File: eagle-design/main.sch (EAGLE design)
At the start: 16 parts, among them IC1 7805T

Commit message: Added new code
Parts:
- added R5, R6: 10K, adafruit:FLIPFLOP-RES
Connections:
- new net VCC: R5.1, R6.1
- net N$7: now also R6.2
- net N$8: now also R5.2
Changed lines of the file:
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@@
 <part name="S1" library="switch-omron" library_urn="urn:adsk.eagle:library:377" deviceset="10-XX" device="" package3d_urn="urn:adsk.eagle:package:27496/1"/>
 <part name="R4" library="adafruit" deviceset="FLIPFLOP-RES" device="" value="10K"/>
+<part name="R5" library="adafruit" deviceset="FLIPFLOP-RES" device="" value="10K"/>
+<part name="R6" library="adafruit" deviceset="FLIPFLOP-RES" device="" value="10K"/>
+<part name="P+1" library="supply1" library_urn="urn:adsk.eagle:library:371" deviceset="VCC" device="" value="3.3V"/>
 </parts>
 <sheets>
@@
 <attribute name="NAME" x="77.2414" y="21.59" size="1.778" layer="95" rot="R90"/>
 <attribute name="VALUE" x="76.962" y="26.67" size="1.778" layer="96" rot="R90"/>
+</instance>
+<instance part="R5" gate="G$1" x="182.88" y="55.88" smashed="yes" rot="R180">
+<attribute name="NAME" x="186.69" y="59.4614" size="1.778" layer="95" rot="R180"/>
+<attribute name="VALUE" x="181.61" y="59.182" size="1.778" layer="96" rot="R180"/>
+</instance>
+<instance part="R6" gate="G$1" x="182.88" y="60.96" smashed="yes" rot="R180">
+<attribute name="NAME" x="186.69" y="64.5414" size="1.778" layer="95" rot="R180"/>
+<attribute name="VALUE" x="181.61" y="64.262" size="1.778" layer="96" rot="R180"/>
+</instance>
+<instance part="P+1" gate="VCC" x="195.58" y="58.42" smashed="yes" rot="R270">
+<attribute name="VALUE" x="193.04" y="60.96" size="1.778" layer="96"/>
 </instance>
 </instances>
@@
 <pinref part="U$1" gate="G$1" pin="D2"/>
 <wire x1="170.18" y1="60.96" x2="135.89" y2="60.96" width="0.1524" layer="91"/>
+<pinref part="R6" gate="G$1" pin="2"/>
+<wire x1="177.8" y1="60.96" x2="170.18" y2="60.96" width="0.1524" layer="91"/>
+<junction x="170.18" y="60.96"/>
 </segment>
 </net>
@@
 <segment>
 <pinref part="U$1" gate="G$1" pin="D1"/>
-<wire x1="135.89" y1="63.5" x2="165.1" y2="63.5" width="0.1524" layer="91"/>
-<wire x1="165.1" y1="63.5" x2="165.1" y2="58.42" width="0.1524" layer="91"/>
+<wire x1="135.89" y1="63.5" x2="162.56" y2="63.5" width="0.1524" layer="91"/>
+<wire x1="162.56" y1="63.5" x2="162.56" y2="58.42" width="0.1524" layer="91"/>
 <pinref part="JP1" gate="A" pin="4"/>
-<wire x1="165.1" y1="58.42" x2="170.18" y2="58.42" width="0.1524" layer="91"/>
+<wire x1="162.56" y1="58.42" x2="170.18" y2="58.42" width="0.1524" layer="91"/>
+<pinref part="R5" gate="G$1" pin="2"/>
+<wire x1="177.8" y1="55.88" x2="175.26" y2="55.88" width="0.1524" layer="91"/>
+<wire x1="175.26" y1="55.88" x2="175.26" y2="58.42" width="0.1524" layer="91"/>
+<wire x1="175.26" y1="58.42" x2="170.18" y2="58.42" width="0.1524" layer="91"/>
+<junction x="170.18" y="58.42"/>
 </segment>
 </net>
@@
 <pinref part="R2" gate="G$1" pin="2"/>
 <wire x1="135.89" y1="55.88" x2="139.7" y2="55.88" width="0.1524" layer="91"/>
-</segment>
-</net>
-<net name="N$9" class="0">
-<segment>
-<pinref part="U$1" gate="G$1" pin="3V3@1"/>
-<pinref part="JP1" gate="A" pin="6"/>
-<wire x1="135.89" y1="53.34" x2="170.18" y2="53.34" width="0.1524" layer="91"/>
 </segment>
 </net>
@@
 </segment>
 </net>
+<net name="N$14" class="0">
+<segment>
+<pinref part="U$1" gate="G$1" pin="3V3@1"/>
+<pinref part="JP1" gate="A" pin="6"/>
+<wire x1="135.89" y1="53.34" x2="170.18" y2="53.34" width="0.1524" layer="91"/>
+</segment>
+</net>
+<net name="VCC" class="0">
+<segment>
+<pinref part="R5" gate="G$1" pin="1"/>
+<pinref part="R6" gate="G$1" pin="1"/>
+<wire x1="187.96" y1="60.96" x2="187.96" y2="58.42" width="0.1524" layer="91"/>
+<wire x1="187.96" y1="58.42" x2="187.96" y2="55.88" width="0.1524" layer="91"/>
+<junction x="187.96" y="58.42"/>
+<pinref part="P+1" gate="VCC" pin="VCC"/>
+<wire x1="193.04" y1="58.42" x2="187.96" y2="58.42" width="0.1524" layer="91"/>
+</segment>
+</net>

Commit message: Added updated eagle design
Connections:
- removed net VCC: R5.1, R6.1
- net N$14: now also R5.1, R6.1
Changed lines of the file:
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@@
 <part name="R5" library="adafruit" deviceset="FLIPFLOP-RES" device="" value="10K"/>
 <part name="R6" library="adafruit" deviceset="FLIPFLOP-RES" device="" value="10K"/>
-<part name="P+1" library="supply1" library_urn="urn:adsk.eagle:library:371" deviceset="VCC" device="" value="3.3V"/>
 </parts>
 <sheets>
@@
 <attribute name="NAME" x="186.69" y="64.5414" size="1.778" layer="95" rot="R180"/>
 <attribute name="VALUE" x="181.61" y="64.262" size="1.778" layer="96" rot="R180"/>
-</instance>
-<instance part="P+1" gate="VCC" x="195.58" y="58.42" smashed="yes" rot="R270">
-<attribute name="VALUE" x="193.04" y="60.96" size="1.778" layer="96"/>
 </instance>
 </instances>
@@
 <pinref part="JP1" gate="A" pin="6"/>
 <wire x1="135.89" y1="53.34" x2="170.18" y2="53.34" width="0.1524" layer="91"/>
-</segment>
-</net>
-<net name="VCC" class="0">
-<segment>
+<wire x1="170.18" y1="53.34" x2="170.18" y2="48.26" width="0.1524" layer="91"/>
+<junction x="170.18" y="53.34"/>
+<wire x1="170.18" y1="48.26" x2="193.04" y2="48.26" width="0.1524" layer="91"/>
 <pinref part="R5" gate="G$1" pin="1"/>
 <pinref part="R6" gate="G$1" pin="1"/>
@@
 <wire x1="187.96" y1="58.42" x2="187.96" y2="55.88" width="0.1524" layer="91"/>
 <junction x="187.96" y="58.42"/>
-<pinref part="P+1" gate="VCC" pin="VCC"/>
 <wire x1="193.04" y1="58.42" x2="187.96" y2="58.42" width="0.1524" layer="91"/>
-</segment>
-</net>
+<wire x1="193.04" y1="48.26" x2="193.04" y2="58.42" width="0.1524" layer="91"/>
+</segment>
+</net>

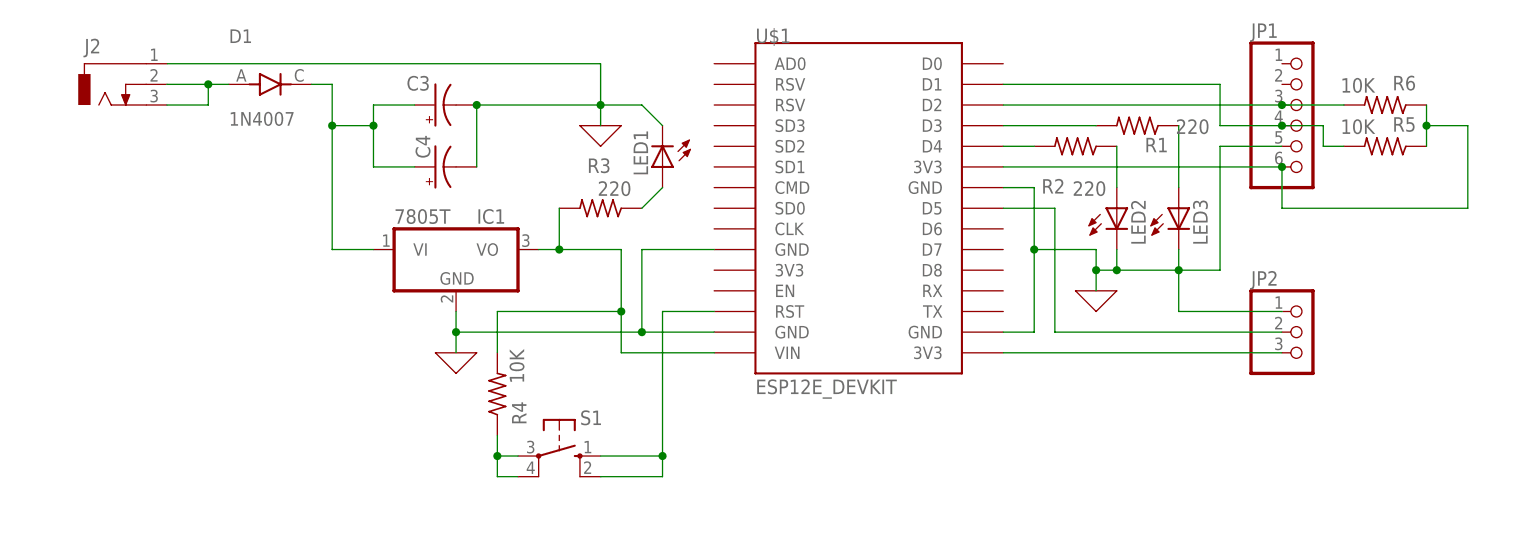
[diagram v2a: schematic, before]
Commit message: Added support for reed switch and rain sensor
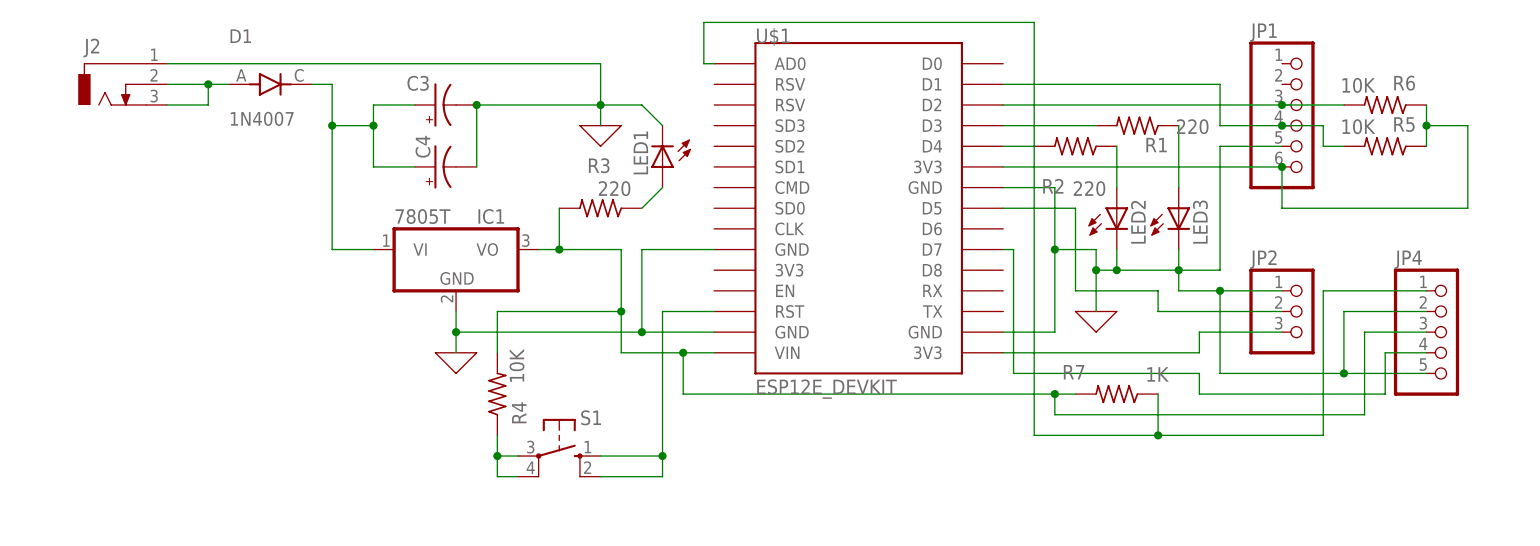
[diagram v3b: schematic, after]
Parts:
- added JP4: (no value), pinhead:PINHD-1X55X2MM
- added R7: 1K, adafruit:FLIPFLOP-RES
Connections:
- new net N$30: IC1.VO, JP4.3, R3.2, R4.2, R7.2, U$1.VIN
- new net N$31: JP4.1, R7.1, U$1.AD0
- net 0: now also JP4.2, JP4.5
- net N$32: now also JP4.4, U$1.D7; no longer IC1.VO, R3.2, R4.2, U$1.VIN
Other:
- moved on the sheet: JP2

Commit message: Micro SD Card reader added to eagle design ; New export images added
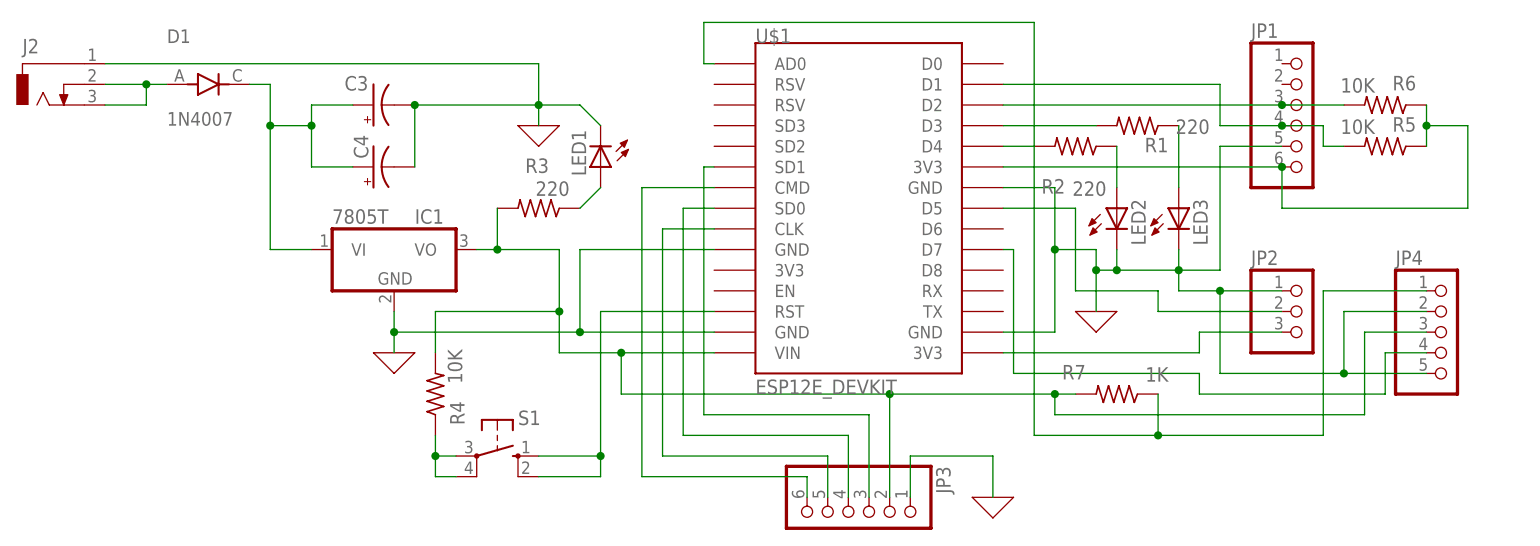
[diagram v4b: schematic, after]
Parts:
- added JP3: (no value), adafruit:PINHD-1X6
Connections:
- new net N$33: JP3.4, U$1.SD0
- new net N$35: JP3.3, U$1.SD1
- new net N$36: JP3.5, U$1.CLK
- new net N$37: JP3.6, U$1.CMD
- net 0: now also JP3.1
- net N$30: now also JP3.2
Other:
- moved on the sheet: C3, C4, D1, IC1, J2, LED1, R3, R4, S1
